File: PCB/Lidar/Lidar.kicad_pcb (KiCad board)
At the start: 2 copper layers, 22.9 x 30.5 mm, 3 parts, among them P1 LIDAR_LEFT, P2 LIDAR_RIGHT, P3 CONN_02X03

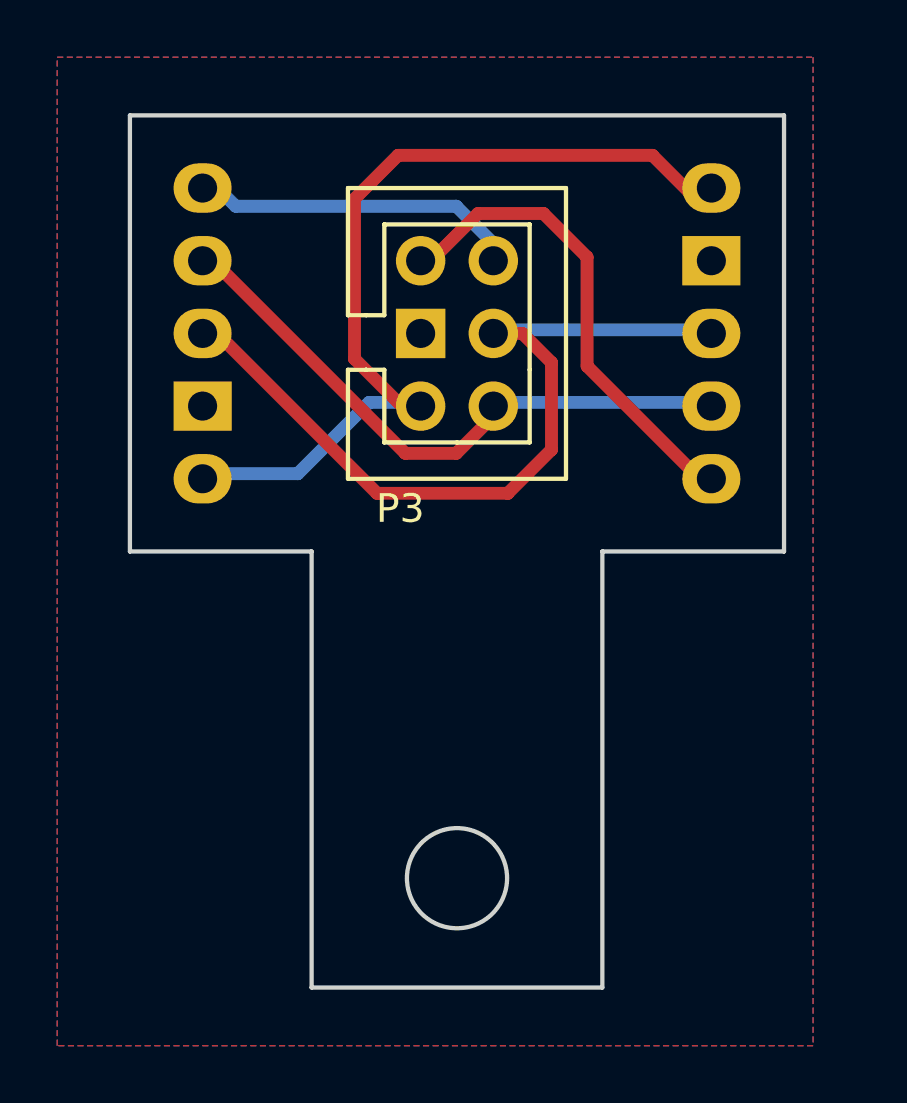
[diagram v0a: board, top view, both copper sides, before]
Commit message: Change lidar PCB
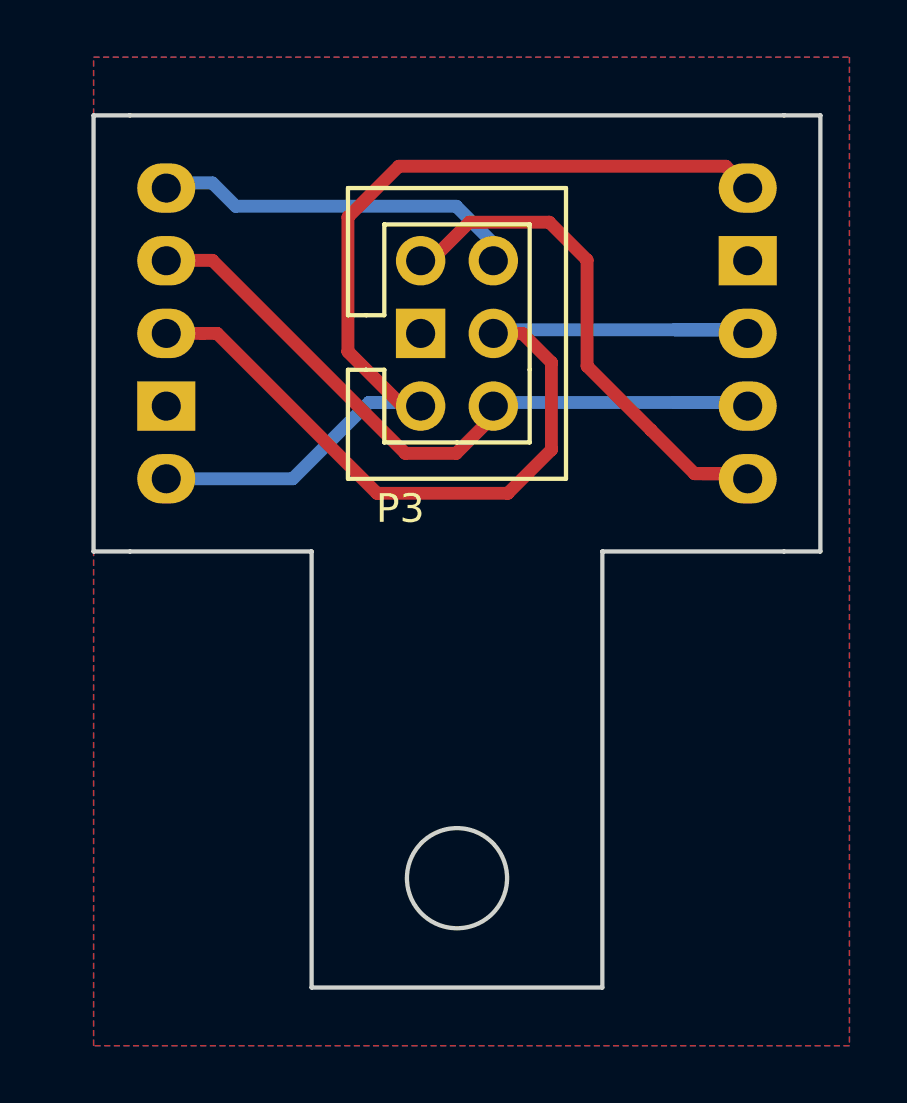
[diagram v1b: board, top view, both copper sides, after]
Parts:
- moved P1 1.27 mm to (83.5, 94.9)
- moved P2 1.27 mm to (103.8, 84.8)
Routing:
- net LID_VIN: track 32.0 -> 38.7 mm
- net LID_SCL: track 21.5 -> 25.5 mm
- net LID_SDA: track 28.1 -> 31.9 mm
- net LID_L_XSHUT: track 11.4 -> 13.1 mm
- net LID_R_XSHUT: track 17.3 -> 18.9 mm
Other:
- board size 22.9 x 30.5 mm -> 25.4 x 30.5 mm
